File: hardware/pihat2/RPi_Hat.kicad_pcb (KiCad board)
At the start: 2 copper layers, 65 x 56 mm, 46 parts, among them J2 RPi_GPIO, P1 USB_OTG, P2 BATT, P3 THERM, U1 MCP73833, U2 SMA_Edge_Mount, U3 SMA_Edge_Mount, U4 TPS61027, U5 MCP3021, U6 Si4464, U7 30MHz

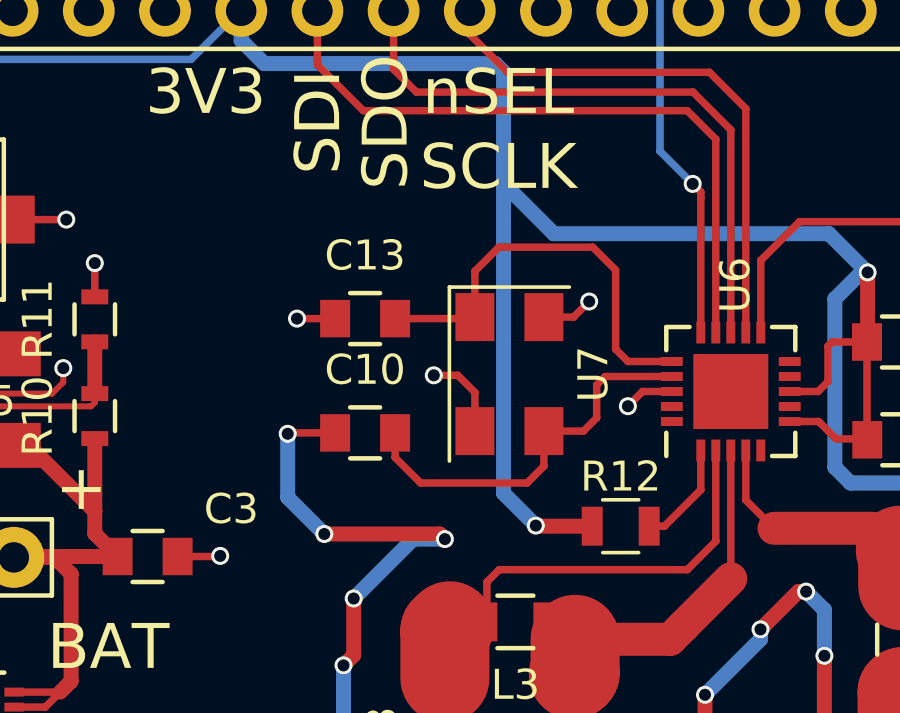
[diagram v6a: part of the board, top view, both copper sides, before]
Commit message: Re-Routed a power trace to provide unbroken ground plane.
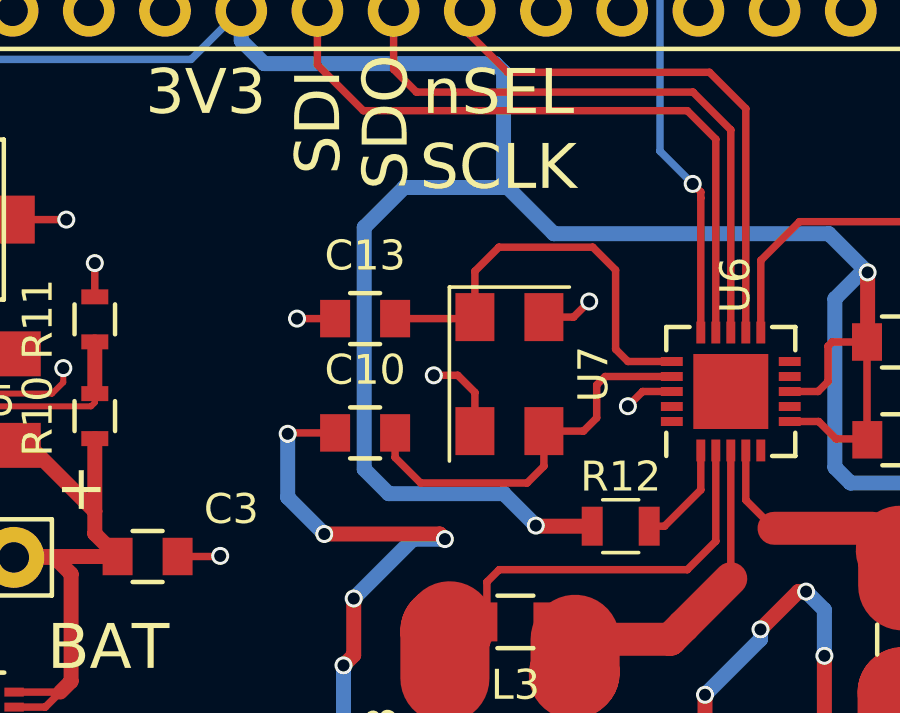
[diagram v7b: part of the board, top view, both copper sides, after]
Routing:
- net +3V3: track 89.1 -> 97.2 mm
- net (no net): track 0.00 -> 4.13 mm, vias 0 -> 2
- net GND: track 199.7 -> 195.5 mm, vias 59 -> 57
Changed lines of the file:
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@@
     (thickness 1.6)
     (drawings 34)
-    (tracks 526)
+    (tracks 531)
     (zones 0)
     (modules 46)
@@
   )
   (setup
-    (last_trace_width 0.25)
+    (last_trace_width 0.5)
     (user_trace_width 0.01)
     (user_trace_width 0.02)
@@
     (visible_elements 7FFEF7FF)
     (pcbplotparams
-      (layerselection 0x010fc_80000001)
+      (layerselection 0x01000_80000001)
       (usegerberextensions true)
       (excludeedgelayer true)
@@
   (gr_line (start 74.74 131.02) (end 74.74 146.52) (layer Edge.Cuts) (width 0.1))
   (gr_line (start 77.74 149.52) (end 136.74 149.52) (angle 90) (layer Edge.Cuts) (width 0.1))
+  (segment (start 106.94 122.96) (end 106.94 124.05) (width 0.25) (layer F.Cu) (net 0))
+  (via (at 108.08 125.19) (size 0.6) (drill 0.4) (layers F.Cu B.Cu) (net 0))
+  (segment (start 106.94 124.05) (end 108.08 125.19) (width 0.25) (layer F.Cu) (net 0))
+  (segment (start 87.55 123.09) (end 87.55 124.52) (width 0.25) (layer B.Cu) (net 0))
+  (via (at 87.55 124.52) (size 0.6) (drill 0.4) (layers F.Cu B.Cu) (net 0))
   (segment (start 76.45098 131.75) (end 76.45098 131.39902) (width 0.25) (layer F.Cu) (net 1))
   (segment (start 76.45098 131.39902) (end 77.3 130.55) (width 0.25) (layer F.Cu) (net 1))
@@
   (segment (start 79.44 104.7) (end 79.45 104.7) (width 0.25) (layer F.Cu) (net 1))
   (segment (start 79.44 104.7) (end 77.4 104.7) (width 0.5) (layer F.Cu) (net 1))
-  (segment (start 106.94 122.96) (end 106.94 124.05) (width 0.25) (layer F.Cu) (net 2))
-  (via (at 108.08 125.19) (size 0.6) (drill 0.4) (layers F.Cu B.Cu) (net 2))
-  (segment (start 106.94 124.05) (end 108.08 125.19) (width 0.25) (layer F.Cu) (net 2))
-  (segment (start 87.55 123.09) (end 87.55 124.52) (width 0.25) (layer B.Cu) (net 2))
-  (via (at 87.55 124.52) (size 0.6) (drill 0.4) (layers F.Cu B.Cu) (net 2))
-  (segment (start 92.76 123) (end 92.76 123.81) (width 0.25) (layer F.Cu) (net 2) (status 400000))
+  (segment (start 92.76 123) (end 92.76 123.81) (width 0.25) (layer F.Cu) (net 2))
   (via (at 91.8 124.09) (size 0.6) (drill 0.4) (layers F.Cu B.Cu) (net 2))
   (segment (start 92.48 124.09) (end 91.8 124.09) (width 0.25) (layer F.Cu) (net 2))
@@
   (via (at 101.25 137.07) (size 0.6) (drill 0.4) (layers F.Cu B.Cu) (net 2))
   (segment (start 99.92 138.4) (end 101.25 137.07) (width 0.5) (layer B.Cu) (net 2))
-  (segment (start 110.22 123.41) (end 107.82 123.41) (width 0.5) (layer F.Cu) (net 2) (status 400000))
+  (segment (start 110.22 123.41) (end 107.82 123.41) (width 0.5) (layer F.Cu) (net 2))
   (segment (start 105.01 112.36) (end 104.98 112.39) (width 0.25) (layer F.Cu) (net 2))
   (via (at 104.98 112.39) (size 0.6) (drill 0.4) (layers F.Cu B.Cu) (net 2))
@@
   (via (at 107.15 122.74) (size 0.6) (drill 0.4) (layers F.Cu B.Cu) (net 2))
   (segment (start 107.82 123.41) (end 107.15 122.74) (width 0.5) (layer F.Cu) (net 2))
-  (segment (start 99.55 145.34) (end 99.55 140.74) (width 0.5) (layer F.Cu) (net 2) (status 400000))
-  (segment (start 110.22 124.09) (end 110.22 123.41) (width 0.5) (layer F.Cu) (net 2) (status 800000))
+  (segment (start 99.55 145.34) (end 99.55 140.74) (width 0.5) (layer F.Cu) (net 2))
+  (segment (start 110.22 124.09) (end 110.22 123.41) (width 0.5) (layer F.Cu) (net 2))
   (segment (start 111.39 125.26) (end 110.22 124.09) (width 0.5) (layer F.Cu) (net 2))
   (via (at 111.39 125.26) (size 0.6) (drill 0.4) (layers F.Cu B.Cu) (net 2))
@@
   (via (at 99.92 140.37) (size 0.6) (drill 0.4) (layers F.Cu B.Cu) (net 2))
   (segment (start 99.55 140.74) (end 99.92 140.37) (width 0.5) (layer F.Cu) (net 2))
-  (segment (start 129.66 145.38) (end 129.66 141.63) (width 0.5) (layer B.Cu) (net 2) (status 400000))
+  (segment (start 129.66 145.38) (end 129.66 141.63) (width 0.5) (layer B.Cu) (net 2))
   (segment (start 128.38 112.59) (end 126.3 112.59) (width 1.1) (layer F.Cu) (net 2))
   (via (at 128.38 112.59) (size 0.6) (drill 0.4) (layers F.Cu B.Cu) (net 2))
@@
   (via (at 128.93 140.9) (size 0.6) (drill 0.4) (layers F.Cu B.Cu) (net 2))
   (segment (start 129.66 141.63) (end 128.93 140.9) (width 0.5) (layer B.Cu) (net 2))
-  (segment (start 107.95 145.34) (end 107.95 142.39) (width 0.5) (layer F.Cu) (net 2) (status 400000))
-  (segment (start 121.26 143.17) (end 121.26 145.38) (width 0.5) (layer B.Cu) (net 2) (status 800000))
+  (segment (start 107.95 145.34) (end 107.95 142.39) (width 0.5) (layer F.Cu) (net 2))
+  (segment (start 121.26 143.17) (end 121.26 145.38) (width 0.5) (layer B.Cu) (net 2))
   (segment (start 122.41 142.02) (end 121.26 143.17) (width 0.5) (layer B.Cu) (net 2))
   (via (at 122.41 142.02) (size 0.6) (drill 0.4) (layers F.Cu B.Cu) (net 2))
@@
   (via (at 108.8 141.54) (size 0.6) (drill 0.4) (layers F.Cu B.Cu) (net 2))
   (segment (start 107.95 142.39) (end 108.8 141.54) (width 0.5) (layer F.Cu) (net 2))
-  (segment (start 88.65 111.95) (end 88.65 114.66) (width 0.25) (layer F.Cu) (net 2) (status 400000))
-  (segment (start 88.16 115.15) (end 86.15 115.15) (width 0.25) (layer F.Cu) (net 2) (status 800000))
+  (segment (start 88.65 111.95) (end 88.65 114.66) (width 0.25) (layer F.Cu) (net 2))
+  (segment (start 88.16 115.15) (end 86.15 115.15) (width 0.25) (layer F.Cu) (net 2))
   (segment (start 88.65 114.66) (end 88.16 115.15) (width 0.25) (layer F.Cu) (net 2))
   (segment (start 128.49 126.82) (end 129.84 126.82) (width 0.25) (layer F.Cu) (net 2))
@@
   (segment (start 125.48 120.25) (end 125.48 120.98) (width 0.5) (layer F.Cu) (net 11))
   (segment (start 125.48 120.98) (end 125.46 121) (width 0.5) (layer F.Cu) (net 11))
+  (segment (start 112.185 114.385) (end 108.345 114.385) (width 0.5) (layer B.Cu) (net 12))
+  (segment (start 108.86 104.18) (end 112.175 104.18) (width 0.5) (layer B.Cu) (net 12))
+  (segment (start 107.53 105.51) (end 108.86 104.18) (width 0.5) (layer B.Cu) (net 12))
+  (segment (start 107.53 113.57) (end 107.53 105.51) (width 0.5) (layer B.Cu) (net 12))
+  (segment (start 108.345 114.385) (end 107.53 113.57) (width 0.5) (layer B.Cu) (net 12))
+  (segment (start 113.27 115.47) (end 115.13 115.47) (width 0.5) (layer F.Cu) (net 12))
+  (segment (start 113.25 115.45) (end 113.27 115.47) (width 0.5) (layer F.Cu) (net 12))
+  (via (at 113.25 115.45) (size 0.6) (drill 0.4) (layers F.Cu B.Cu) (net 12))
+  (segment (start 112.175 114.375) (end 112.185 114.385) (width 0.5) (layer B.Cu) (net 12))
+  (segment (start 112.185 114.385) (end 113.25 115.45) (width 0.5) (layer B.Cu) (net 12))
   (segment (start 124.31 107.01) (end 124.1 107.01) (width 0.5) (layer B.Cu) (net 12))
   (segment (start 127.97 114.03) (end 127.97 115.59) (width 0.5) (layer F.Cu) (net 12))
@@
   (segment (start 124.31 109.31) (end 124.31 107.01) (width 0.5) (layer F.Cu) (net 12))
   (segment (start 112.31 104.18) (end 113.85 105.72) (width 0.5) (layer B.Cu) (net 12))
+  (segment (start 112.31 104.18) (end 112.175 104.18) (width 0.5) (layer B.Cu) (net 12))
+  (segment (start 123.02 105.72) (end 124.31 107.01) (width 0.5) (layer B.Cu) (net 12))
   (segment (start 113.85 105.72) (end 123.02 105.72) (width 0.5) (layer B.Cu) (net 12))
-  (segment (start 123.02 105.72) (end 124.31 107.01) (width 0.5) (layer B.Cu) (net 12))
   (via (at 124.31 107.01) (size 0.6) (drill 0.4) (layers F.Cu B.Cu) (net 12))
-  (segment (start 112.31 104.18) (end 112.175 104.18) (width 0.5) (layer B.Cu) (net 12))
   (segment (start 124.31 109.31) (end 124.29 109.33) (width 0.5) (layer F.Cu) (net 12))
   (segment (start 112.175 100.325) (end 112.175 104.18) (width 0.5) (layer B.Cu) (net 12))
-  (segment (start 112.175 104.18) (end 112.175 114.375) (width 0.5) (layer B.Cu) (net 12))
-  (segment (start 112.175 114.375) (end 113.25 115.45) (width 0.5) (layer B.Cu) (net 12))
-  (via (at 113.25 115.45) (size 0.6) (drill 0.4) (layers F.Cu B.Cu) (net 12))
-  (segment (start 113.25 115.45) (end 113.27 115.47) (width 0.5) (layer F.Cu) (net 12))
-  (segment (start 113.27 115.47) (end 115.13 115.47) (width 0.5) (layer F.Cu) (net 12))
   (segment (start 124.29 109.33) (end 124.29 112.39) (width 0.25) (layer F.Cu) (net 12))
   (segment (start 124.29 112.39) (end 124.12 112.56) (width 0.25) (layer F.Cu) (net 12))

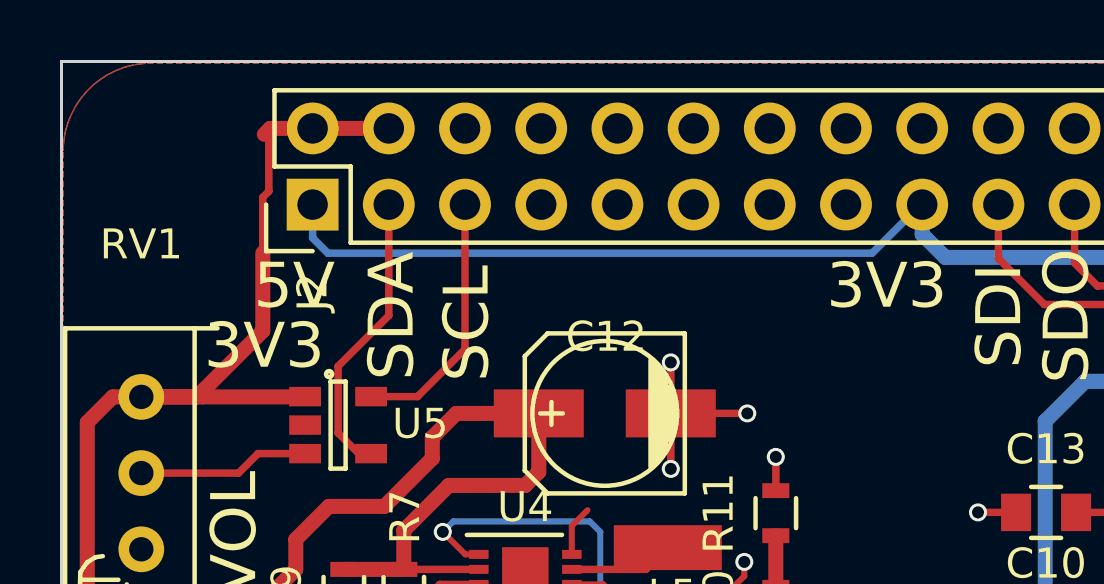
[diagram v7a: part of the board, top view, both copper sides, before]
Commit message: Changed 5V Trace Size
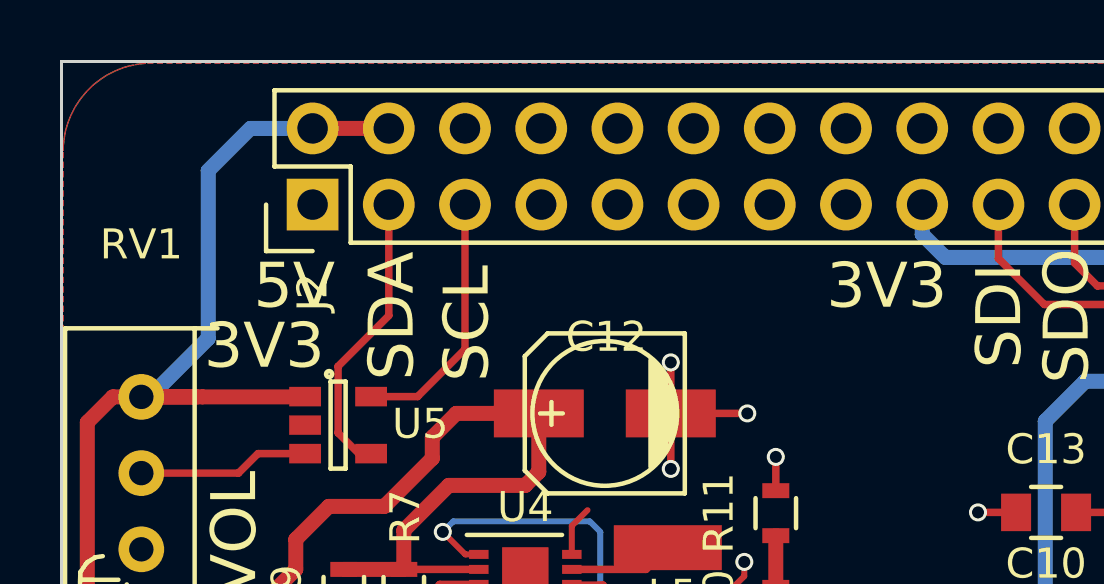
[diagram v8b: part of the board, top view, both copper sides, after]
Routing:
- net +3V3: track 97.2 -> 74.9 mm
- net 5VU: track 104.9 -> 106.1 mm
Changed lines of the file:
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@@
   (general
     (links 117)
-    (no_connects 5)
+    (no_connects 6)
     (area 74.584999 93.469999 139.790001 151.255)
     (thickness 1.6)
     (drawings 34)
-    (tracks 531)
+    (tracks 524)
     (zones 0)
     (modules 46)
@@
     (add_net nSEL)
   )
-  (module Housings_DFN_QFN:DFN-10-1EP_3x3mm_Pitch0.5mm (layer F.Cu)
-    (at 90.2 110.95)
-    (descr "10-Lead Plastic Dual Flat, No Lead Package (MF) - 3x3x0.9 mm Body [DFN] (see Microchip Packaging Specification 00000049BS.pdf)")
-    (tags "DFN 0.5")
-    (attr smd)
-    (fp_text reference U4 (at 0 -2.575) (layer F.SilkS)
-      (effects (font (size 1 1) (thickness 0.15)))
-    )
-    (fp_text value TPS61027 (at 0 2.575) (layer F.Fab)
-      (effects (font (size 1 1) (thickness 0.15)))
-    )
-    (fp_line (start -2.15 -1.85) (end -2.15 1.85) (layer F.CrtYd) (width 0.05))
-    (fp_line (start 2.15 -1.85) (end 2.15 1.85) (layer F.CrtYd) (width 0.05))
-    (fp_line (start -2.15 -1.85) (end 2.15 -1.85) (layer F.CrtYd) (width 0.05))
-    (fp_line (start -2.15 1.85) (end 2.15 1.85) (layer F.CrtYd) (width 0.05))
-    (fp_line (start -1.225 1.65) (end 1.225 1.65) (layer F.SilkS) (width 0.15))
-    (fp_line (start -1.95 -1.65) (end 1.225 -1.65) (layer F.SilkS) (width 0.15))
-    (pad 1 smd rect (at -1.55 -1) (size 0.65 0.3) (layers F.Cu F.Paste F.Mask)
-      (net 3 VBAT))
-    (pad 2 smd rect (at -1.55 -0.5) (size 0.65 0.3) (layers F.Cu F.Paste F.Mask)
-      (net 1 5VU))
-    (pad 3 smd rect (at -1.55 0) (size 0.65 0.3) (layers F.Cu F.Paste F.Mask)
-      (net 20 "Net-(R7-Pad2)"))
-    (pad 4 smd rect (at -1.55 0.5) (size 0.65 0.3) (layers F.Cu F.Paste F.Mask)
-      (net 21 "Net-(R9-Pad1)"))
-    (pad 5 smd rect (at -1.55 1) (size 0.65 0.3) (layers F.Cu F.Paste F.Mask)
-      (net 2 GND))
-    (pad 6 smd rect (at 1.55 1) (size 0.65 0.3) (layers F.Cu F.Paste F.Mask)
-      (net 3 VBAT))
-    (pad 7 smd rect (at 1.55 0.5) (size 0.65 0.3) (layers F.Cu F.Paste F.Mask)
-      (net 22 "Net-(R10-Pad2)"))
-    (pad 8 smd rect (at 1.55 0) (size 0.65 0.3) (layers F.Cu F.Paste F.Mask)
-      (net 2 GND))
-    (pad 9 smd rect (at 1.55 -0.5) (size 0.65 0.3) (layers F.Cu F.Paste F.Mask)
-      (net 16 "Net-(L5-Pad1)"))
-    (pad 10 smd rect (at 1.55 -1) (size 0.65 0.3) (layers F.Cu F.Paste F.Mask)
-      (net 2 GND))
-    (pad 11 smd rect (at 0.3875 0.62) (size 0.775 1.24) (layers F.Cu F.Paste F.Mask)
-      (solder_paste_margin_ratio -0.2))
-    (pad 11 smd rect (at 0.3875 -0.62) (size 0.775 1.24) (layers F.Cu F.Paste F.Mask)
-      (solder_paste_margin_ratio -0.2))
-    (pad 11 smd rect (at -0.3875 0.62) (size 0.775 1.24) (layers F.Cu F.Paste F.Mask)
-      (solder_paste_margin_ratio -0.2))
-    (pad 11 smd rect (at -0.3875 -0.62) (size 0.775 1.24) (layers F.Cu F.Paste F.Mask)
-      (solder_paste_margin_ratio -0.2))
-    (model Housings_DFN_QFN.3dshapes/DFN-10-1EP_3x3mm_Pitch0.5mm.wrl
-      (at (xyz 0 0 0))
-      (scale (xyz 1 1 1))
-      (rotate (xyz 0 0 0))
-    )
-  )
   (module RPi_Hat:Pin_Header_Straight_2x20 (layer F.Cu)
     (at 107.24 97.02 90)
@@
       (scale (xyz 1 1 1))
       (rotate (xyz 0 0 90))
+    )
+  )
+  (module Housings_DFN_QFN:DFN-10-1EP_3x3mm_Pitch0.5mm (layer F.Cu)
+    (at 90.2 110.95)
+    (descr "10-Lead Plastic Dual Flat, No Lead Package (MF) - 3x3x0.9 mm Body [DFN] (see Microchip Packaging Specification 00000049BS.pdf)")
+    (tags "DFN 0.5")
+    (attr smd)
+    (fp_text reference U4 (at 0 -2.575) (layer F.SilkS)
+      (effects (font (size 1 1) (thickness 0.15)))
+    )
+    (fp_text value TPS61027 (at 0 2.575) (layer F.Fab)
+      (effects (font (size 1 1) (thickness 0.15)))
+    )
+    (fp_line (start -2.15 -1.85) (end -2.15 1.85) (layer F.CrtYd) (width 0.05))
+    (fp_line (start 2.15 -1.85) (end 2.15 1.85) (layer F.CrtYd) (width 0.05))
+    (fp_line (start -2.15 -1.85) (end 2.15 -1.85) (layer F.CrtYd) (width 0.05))
+    (fp_line (start -2.15 1.85) (end 2.15 1.85) (layer F.CrtYd) (width 0.05))
+    (fp_line (start -1.225 1.65) (end 1.225 1.65) (layer F.SilkS) (width 0.15))
+    (fp_line (start -1.95 -1.65) (end 1.225 -1.65) (layer F.SilkS) (width 0.15))
+    (pad 1 smd rect (at -1.55 -1) (size 0.65 0.3) (layers F.Cu F.Paste F.Mask)
+      (net 3 VBAT))
+    (pad 2 smd rect (at -1.55 -0.5) (size 0.65 0.3) (layers F.Cu F.Paste F.Mask)
+      (net 1 5VU))
+    (pad 3 smd rect (at -1.55 0) (size 0.65 0.3) (layers F.Cu F.Paste F.Mask)
+      (net 20 "Net-(R7-Pad2)"))
+    (pad 4 smd rect (at -1.55 0.5) (size 0.65 0.3) (layers F.Cu F.Paste F.Mask)
+      (net 21 "Net-(R9-Pad1)"))
+    (pad 5 smd rect (at -1.55 1) (size 0.65 0.3) (layers F.Cu F.Paste F.Mask)
+      (net 2 GND))
+    (pad 6 smd rect (at 1.55 1) (size 0.65 0.3) (layers F.Cu F.Paste F.Mask)
+      (net 3 VBAT))
+    (pad 7 smd rect (at 1.55 0.5) (size 0.65 0.3) (layers F.Cu F.Paste F.Mask)
+      (net 22 "Net-(R10-Pad2)"))
+    (pad 8 smd rect (at 1.55 0) (size 0.65 0.3) (layers F.Cu F.Paste F.Mask)
+      (net 2 GND))
+    (pad 9 smd rect (at 1.55 -0.5) (size 0.65 0.3) (layers F.Cu F.Paste F.Mask)
+      (net 16 "Net-(L5-Pad1)"))
+    (pad 10 smd rect (at 1.55 -1) (size 0.65 0.3) (layers F.Cu F.Paste F.Mask)
+      (net 2 GND))
+    (pad 11 smd rect (at 0.3875 0.62) (size 0.775 1.24) (layers F.Cu F.Paste F.Mask)
+      (solder_paste_margin_ratio -0.2))
+    (pad 11 smd rect (at 0.3875 -0.62) (size 0.775 1.24) (layers F.Cu F.Paste F.Mask)
+      (solder_paste_margin_ratio -0.2))
+    (pad 11 smd rect (at -0.3875 0.62) (size 0.775 1.24) (layers F.Cu F.Paste F.Mask)
+      (solder_paste_margin_ratio -0.2))
+    (pad 11 smd rect (at -0.3875 -0.62) (size 0.775 1.24) (layers F.Cu F.Paste F.Mask)
+      (solder_paste_margin_ratio -0.2))
+    (model Housings_DFN_QFN.3dshapes/DFN-10-1EP_3x3mm_Pitch0.5mm.wrl
+      (at (xyz 0 0 0))
+      (scale (xyz 1 1 1))
+      (rotate (xyz 0 0 0))
     )
   )
@@
   (segment (start 87.55 123.09) (end 87.55 124.52) (width 0.25) (layer B.Cu) (net 0))
   (via (at 87.55 124.52) (size 0.6) (drill 0.4) (layers F.Cu B.Cu) (net 0))
+  (segment (start 77.4 104.7) (end 77.68 104.7) (width 0.5) (layer B.Cu) (net 1))
+  (segment (start 77.68 104.7) (end 79.63 102.75) (width 0.5) (layer B.Cu) (net 1))
+  (segment (start 81.04 95.75) (end 83.11 95.75) (width 0.5) (layer B.Cu) (net 1))
+  (segment (start 79.63 97.16) (end 81.04 95.75) (width 0.5) (layer B.Cu) (net 1))
+  (segment (start 79.63 102.75) (end 79.63 97.16) (width 0.5) (layer B.Cu) (net 1))
   (segment (start 76.45098 131.75) (end 76.45098 131.39902) (width 0.25) (layer F.Cu) (net 1))
   (segment (start 76.45098 131.39902) (end 77.3 130.55) (width 0.25) (layer F.Cu) (net 1))
@@
   (segment (start 90.2 107.65) (end 90.65036 107.19964) (width 0.5) (layer F.Cu) (net 1))
   (segment (start 90.65036 107.19964) (end 90.65036 105.25) (width 0.5) (layer F.Cu) (net 1))
-  (segment (start 81.45 99.9) (end 81.45 98.05) (width 0.25) (layer F.Cu) (net 1))
-  (segment (start 79.25 104.7) (end 81.45 102.5) (width 0.5) (layer F.Cu) (net 1))
-  (segment (start 81.45 102.5) (end 81.45 99.9) (width 0.5) (layer F.Cu) (net 1))
   (segment (start 77.4 104.7) (end 79.25 104.7) (width 0.5) (layer F.Cu) (net 1))
-  (segment (start 81.7 95.75) (end 81.5 95.95) (width 0.5) (layer F.Cu) (net 1))
-  (segment (start 81.7 95.75) (end 83.11 95.75) (width 0.5) (layer F.Cu) (net 1))
-  (segment (start 81.65 96.1) (end 81.5 95.95) (width 0.25) (layer F.Cu) (net 1))
-  (segment (start 81.65 97.85) (end 81.65 96.1) (width 0.25) (layer F.Cu) (net 1))
-  (segment (start 81.45 98.05) (end 81.65 97.85) (width 0.25) (layer F.Cu) (net 1))
   (segment (start 84.15 110.45) (end 86.15 110.45) (width 0.5) (layer F.Cu) (net 1))
   (segment (start 86.15 110.45) (end 88.65 110.45) (width 0.25) (layer F.Cu) (net 1))
@@
   (segment (start 123.26 112.56) (end 122.68 111.98) (width 0.25) (layer F.Cu) (net 12))
   (segment (start 103.43 98.29) (end 103.38 98.29) (width 0.25) (layer B.Cu) (net 12))
-  (segment (start 103.38 98.29) (end 101.76 99.91) (width 0.25) (layer B.Cu) (net 12))
-  (segment (start 83.11 99.4) (end 83.11 98.29) (width 0.25) (layer B.Cu) (net 12))
-  (segment (start 83.62 99.91) (end 83.11 99.4) (width 0.25) (layer B.Cu) (net 12))
-  (segment (start 101.76 99.91) (end 83.62 99.91) (width 0.25) (layer B.Cu) (net 12))
   (segment (start 103.43 98.29) (end 103.43 99.28) (width 0.5) (layer B.Cu) (net 12))
   (segment (start 111.9 100.05) (end 112.175 100.325) (width 0.5) (layer B.Cu) (net 12))
